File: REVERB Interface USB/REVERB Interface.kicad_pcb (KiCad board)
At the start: 2 copper layers, 90.2 x 95.9 mm, 74 parts, among them J1 RPiZeroW, J2 Iridium, J3 APRS, J4 Antenna, J6 USB_B_Micro, J7 USB, J8 USBPOGO, M1 MountingHole_Pad, M2 MountingHole_Pad, M3 MountingHole_Pad, M4 MountingHole_Pad, M5 PiMount, M6 PiMount, M7 PiMount, M8 PiMount, U1 IMU, U2 MAX3232, U3 CY7C65213-28PVXI, U4 TXB0104D

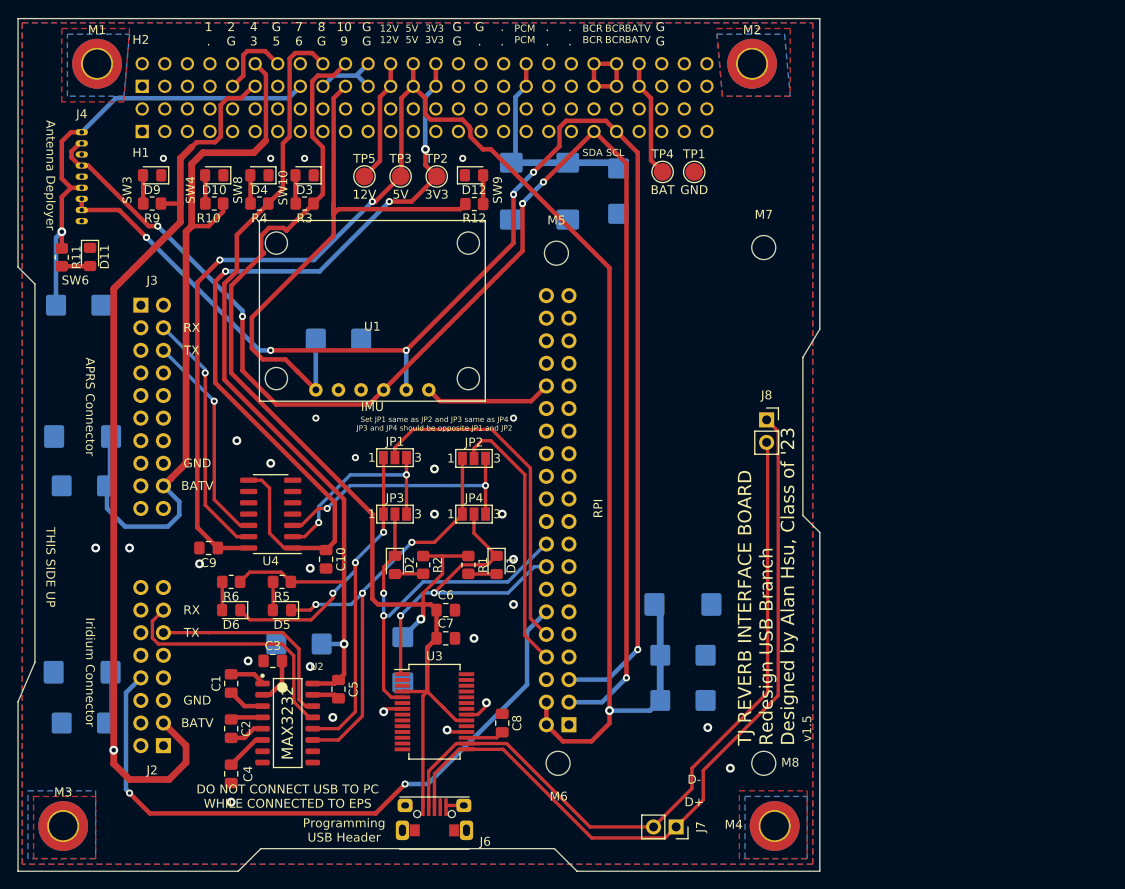
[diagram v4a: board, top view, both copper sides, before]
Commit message: implement rtc on a pdm
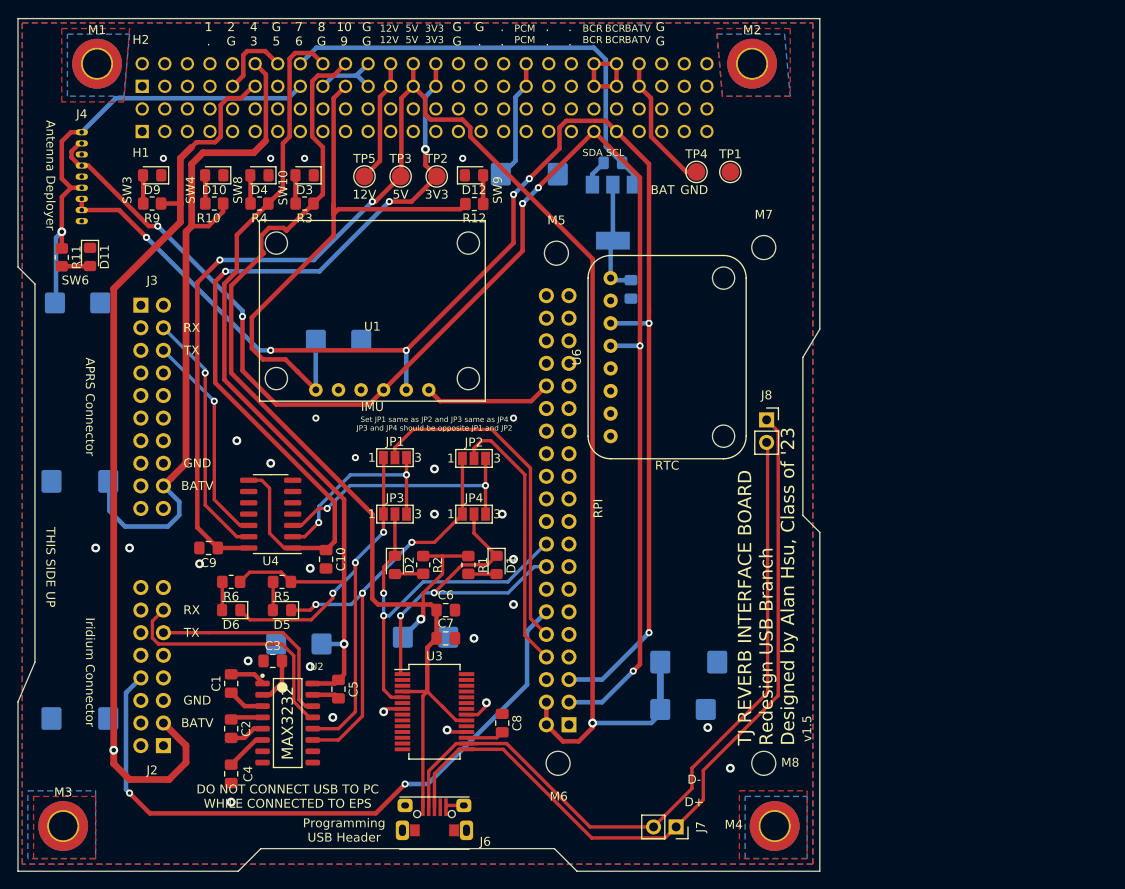
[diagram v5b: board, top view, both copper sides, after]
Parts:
- removed C22, C24, C25, C27: 47uF, Capacitor_Tantalum_SMD:CP_EIA-6032-28_Kemet-C_Pad2.25x2.35mm_HandSolder
- removed C23: 100uF, Capacitor_Tantalum_SMD:CP_EIA-7343-43_Kemet-X_Pad2.25x2.55mm_HandSolder
- added C17: 22uF, Capacitor_Tantalum_SMD:CP_EIA-6032-28_Kemet-C_Pad2.25x2.35mm_HandSolder, B.Cu at (138.4, 123.2)
- added C19: 22uF, Capacitor_Tantalum_SMD:CP_EIA-6032-28_Kemet-C_Pad2.25x2.35mm_HandSolder, B.Cu at (152.7, 122.4)
- added U5: LM1117-3.3, Package_TO_SOT_SMD:SOT-223-3_TabPin2, B.Cu at (173.7, 74.7)
- added U6: DS3231BOB, REVERB Interface:DS3231BOB, F.Cu at (173.5, 90.9)
- C12, C15: value 47uF -> 100uF; footprint Capacitor_Tantalum_SMD:CP_EIA-6032-28_Kemet-C_Pad2.25x2.35mm_HandSolder -> Capacitor_Tantalum_SMD:CP_EIA-7343-43_Kemet-X_Pad2.25x2.55mm_HandSolder
- C13: value 22uF -> 47uF
- C18: value 47uF -> 22uF
- C20, C21: value 100uF -> 10uF; footprint Capacitor_Tantalum_SMD:CP_EIA-7343-43_Kemet-X_Pad2.25x2.55mm_HandSolder -> Capacitor_SMD:C_0805_2012Metric_Pad1.18x1.45mm_HandSolder
- moved C12 56.8 mm to (164.3, 70.4)
- moved C15 27.2 mm to (113.8, 104.9)
- moved C21 13.1 mm to (175.8, 83.3)
- moved C20 11.9 mm to (173.7, 69.1), turned to 180 degrees
- moved C11 6.51 mm to (182.3, 125.2)
- moved C14 5.21 mm to (113.8, 131.6)
- moved TP1 4.06 mm to (186.9, 70.1)
- moved TP4 3.81 mm to (183.1, 70.1)
- moved C13 1.02 mm to (181.6, 130.6)
- moved C16 0.28 mm to (113.5, 84.8)
- moved C18 0.13 mm to (142.9, 89.0)
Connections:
- C12 pad 1: +5V -> /PCM_IN
- C15 pad 1: /SW3 -> /SW4
- C20 pad 1: /PCM_IN -> /SW7
- C21 pad 1: /PCM_IN -> Net-(C21-Pad1)
- H2 pad 16: (no net) -> /SW7
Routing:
- net /SW7: track 0.00 -> 51.0 mm
- net Net-(C21-Pad1): track 0.00 -> 13.0 mm
- net /PCM_IN: track 24.2 -> 13.9 mm
- net +5V: track 187.2 -> 180.4 mm
- net /SW4: track 83.0 -> 77.3 mm
- net /SW3: track 114.2 -> 108.9 mm
- net /EPSSCL: track 156.5 -> 161.5 mm, vias 6 -> 7
- net /EPSSDA: track 162.9 -> 167.4 mm, vias 5 -> 6
- net GND: track 29.4 -> 32.4 mm
- net VBUS: track 13.3 -> 15.5 mm
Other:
- board text added: "RTC"

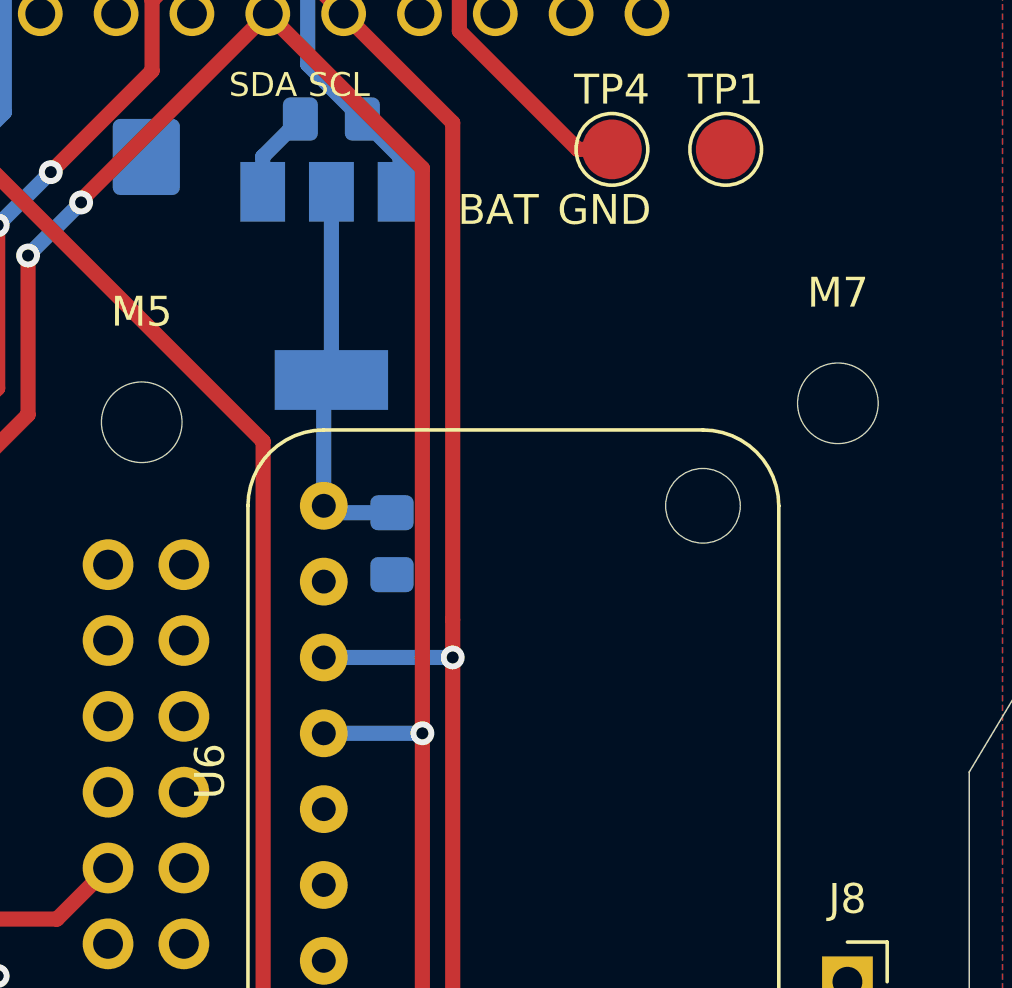
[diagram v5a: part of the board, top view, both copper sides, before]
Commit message: embed the rtc
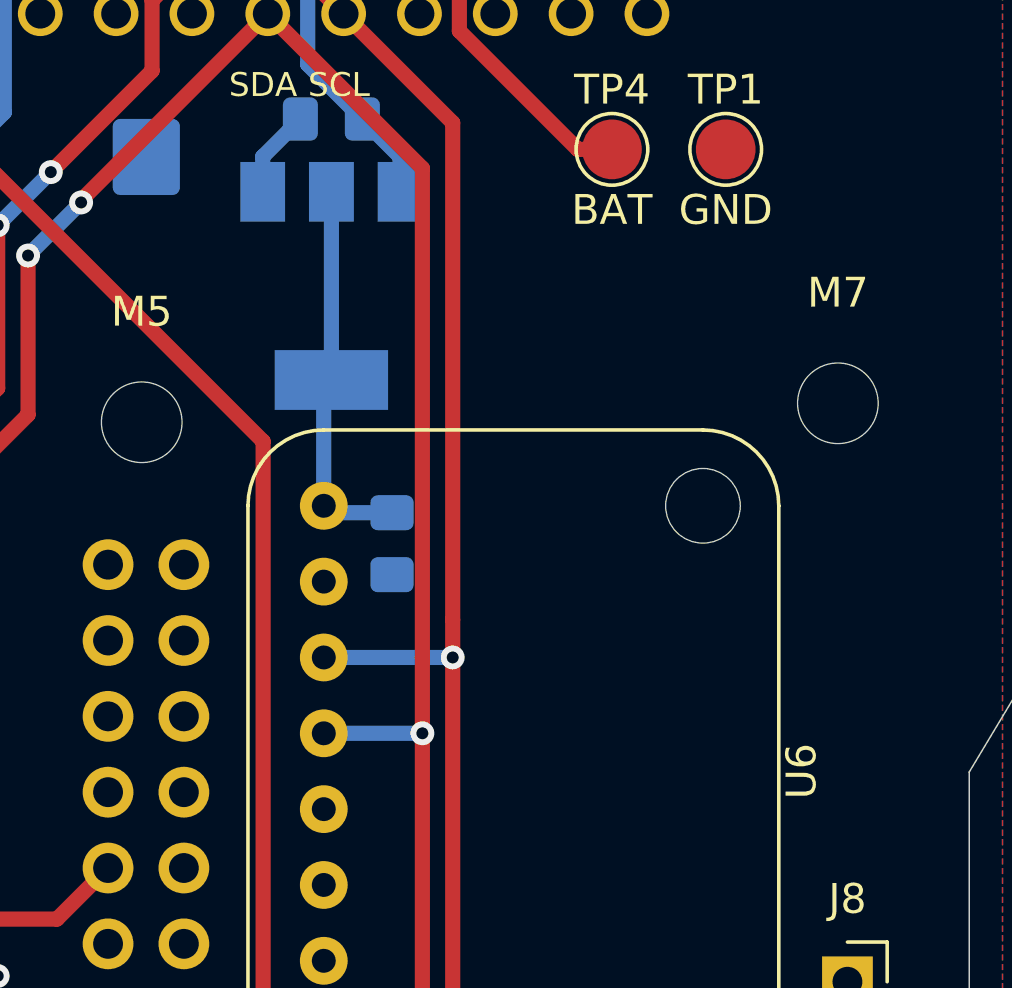
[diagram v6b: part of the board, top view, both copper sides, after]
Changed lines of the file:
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@@
   (module "REVERB Interface:DS3231BOB" (layer F.Cu)
     (at 173.482 90.932 270)
-    (fp_text reference U6 (at 0 3.81 90) (layer F.SilkS)
+    (fp_text reference U6 (at 0 -16.002 90) (layer F.SilkS)
       (effects (font (size 1 1) (thickness 0.15)))
     )
@@
     (effects (font (size 1 1) (thickness 0.15)))
   )
-  (gr_text GND (at 182.88 72.136) (layer F.SilkS)
+  (gr_text GND (at 186.944 72.136) (layer F.SilkS)
     (effects (font (size 1 1) (thickness 0.15)))
   )
-  (gr_text BAT (at 179.324 72.136) (layer F.SilkS)
+  (gr_text BAT (at 183.134 72.136) (layer F.SilkS)
     (effects (font (size 1 1) (thickness 0.15)))
   )

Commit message: 3d model updates
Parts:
- removed U6: DS3231BOB, REVERB Interface:DS3231BOB
- added BT1: CR-2032, REVERB Interface:CR2032-LINX-HLD-001-THM, F.Cu at (209.6, 87.6)
- added TP6: SQWV, TestPoint:TestPoint_Pad_D2.0mm, F.Cu at (223.6, 89.9)
- C20: value 10uF -> 1uF
- C21: value 10uF -> 1uF; moved to F.Cu
- U5: value LM1117-3.3 -> DS3232M; footprint Package_TO_SOT_SMD:SOT-223-3_TabPin2 -> Package_SO:SOIC-8_3.9x4.9mm_P1.27mm; moved to F.Cu
- moved U5 52.5 mm to (225.8, 81.6), turned to 0 degrees
- moved C21 48.3 mm to (224.0, 86.3), turned to 0 degrees
- moved C20 22.4 mm to (184.2, 88.9)
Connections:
- C20 pad 1: /SW7 -> +3V3
- C21 pad 1: Net-(C21-Pad1) -> Net-(BT1-Pad1)
- H2 pad 16: /SW7 -> (no net)
- U5 pad 1: GND -> (no net)
- U5 pad 2: Net-(C21-Pad1) -> +3V3
- U5 pad 3: /SW7 -> /SQW
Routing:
- net /SW7: track 51.0 -> 0.00 mm
- net Net-(C21-Pad1): track 13.0 -> 0.00 mm
- net /EPSSCL: track 161.5 -> 157.2 mm, vias 7 -> 6
- net /EPSSDA: track 167.4 -> 164.1 mm, vias 6 -> 5
- net GND: track 32.4 -> 29.4 mm

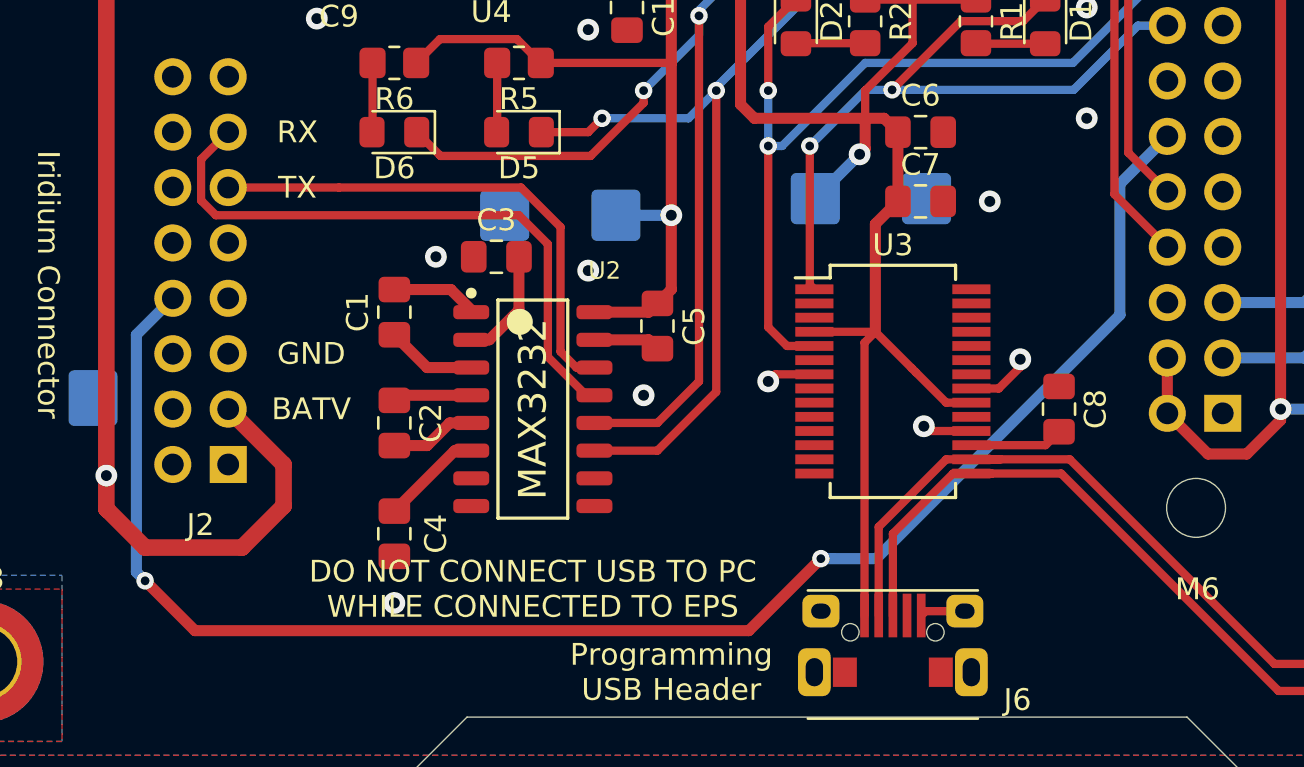
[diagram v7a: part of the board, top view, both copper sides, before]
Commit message: Remove RI line
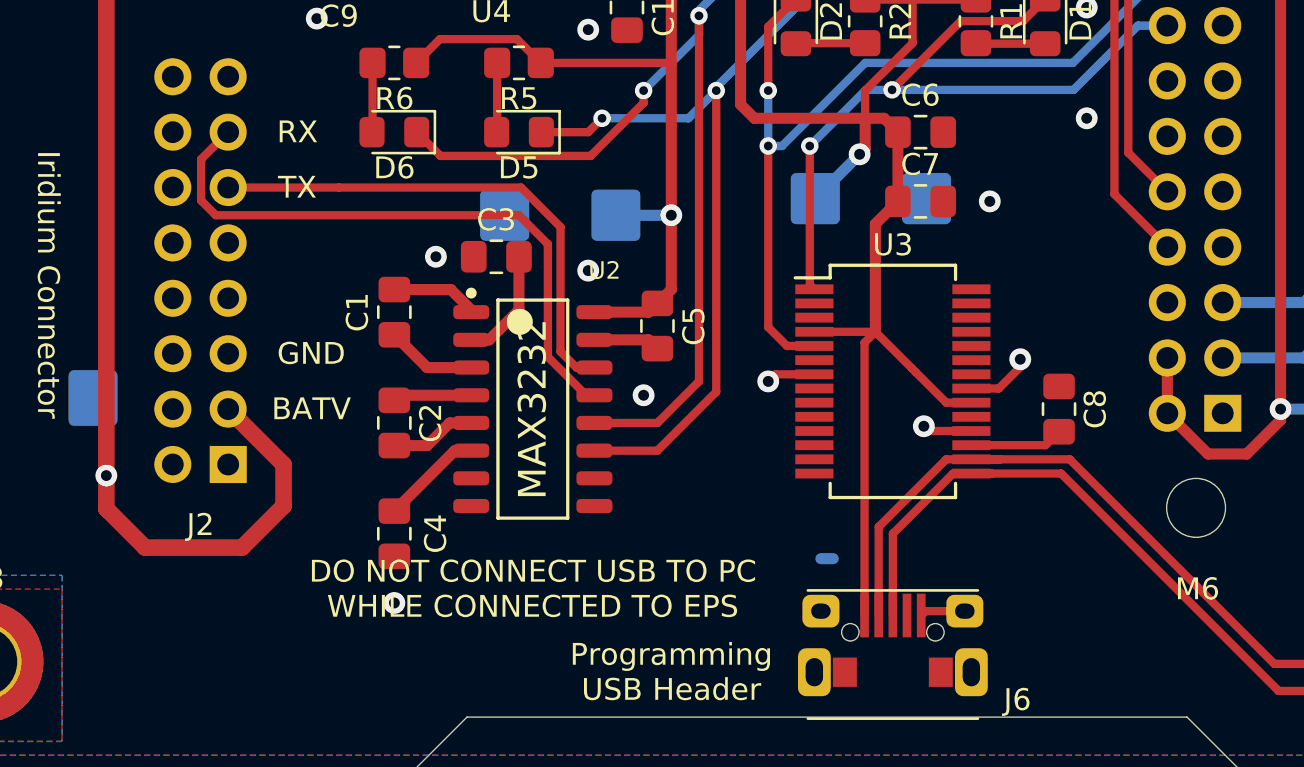
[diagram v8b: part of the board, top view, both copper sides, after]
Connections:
- J1 pad 12: /RI -> (no net)
- J2 pad 8: /RI -> (no net)
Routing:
- net /RI: track 74.5 -> 0.57 mm, vias 2 -> 0
